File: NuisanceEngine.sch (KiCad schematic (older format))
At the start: 60 parts, among them J1 1/8\" Stereo, J2 CV_IN, J3 PWR_IN, J4 GND, J5 PWR_NORM, Q1 2N3904, Q2 2N3904, Q3 TIP31A, Q4 TIP32A, SW1 SW_SPDT, SW2 SW_SPDT, U1 LM324

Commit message: Made footprint for second model of battery holder
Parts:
- BT1: footprint (none) -> HammerheadAudio:9V_Clip
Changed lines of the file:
@@
 F 0 "BT1" H 10750 2200 50  0000 L CNN
 F 1 "9V_Battery" H 10750 2100 50  0000 L CNN
-F 2 "" V 10650 2160 50  0001 C CNN
+F 2 "HammerheadAudio:9V_Clip" V 10650 2160 50  0001 C CNN
 F 3 "" V 10650 2160 50  0001 C CNN
 	1    10650 2100

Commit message: Updated to Kicad 5... Very annoying >:/
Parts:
- removed J1: 1/8\" Stereo, HammerheadAudio:EuroJack_StereoTHT, symbol Audio-Jack-3
- removed J2: CV_IN, HammerheadAudio:EuroJack_MonoSW_THT, symbol Audio-Jack-2_Switch
- added J1, J8: GND, Connector_PinHeader_2.54mm:PinHeader_1x01_P2.54mm_Vertical, symbol Connector:Conn_01x01_Female
- added J2: CV, Connector_PinHeader_2.54mm:PinHeader_1x01_P2.54mm_Vertical, symbol Connector:Conn_01x01_Female
- added J6: L, Connector_PinHeader_2.54mm:PinHeader_1x01_P2.54mm_Vertical, symbol Connector:Conn_01x01_Female
- added J7: R, Connector_PinHeader_2.54mm:PinHeader_1x01_P2.54mm_Vertical, symbol Connector:Conn_01x01_Female
- added unit 5 of U1
- BT1: symbol Battery_Cell -> Device:Battery_Cell
- C1, C2, C3, C4, C5, C6, C7: symbol C -> Device:C
- C10, C11, C8, C9: symbol CP -> Device:CP
- D1: symbol D -> Device:D
- D2: symbol LED -> Device:LED
- J3: value PWR_IN -> 9V; footprint Pin_Headers:Pin_Header_Straight_1x01_Pitch2.54mm -> Connector_PinHeader_2.54mm:PinHeader_1x01_P2.54mm_Vertical; symbol Conn_01x01 -> Connector:Conn_01x01_Female
- J4: footprint Pin_Headers:Pin_Header_Straight_1x01_Pitch2.54mm -> Connector_PinHeader_2.54mm:PinHeader_1x01_P2.54mm_Vertical; symbol Conn_01x01 -> Connector:Conn_01x01_Female
- J5: value PWR_NORM -> BAT; footprint Pin_Headers:Pin_Header_Straight_1x01_Pitch2.54mm -> Connector_PinHeader_2.54mm:PinHeader_1x01_P2.54mm_Vertical; symbol Conn_01x01 -> Connector:Conn_01x01_Female
- LS1: symbol Speaker -> Device:Speaker
- Q1: symbol Q_NPN_EBC -> Device:Q_NPN_EBC
- Q2: symbol Q_NPN_EBC -> Transistor_BJT:2N3904
- Q3: symbol TIP41 -> Device:Q_NPN_BCE
- Q4: symbol Q_PNP_BCE -> Device:Q_PNP_BCE
- R1, R10, R11, R12, R13, R14, R15, R16, R17, R18, R19, R2, R20, R21, R22, R23, R24, R25, R26, R27, R29, R3, R4, R5, R6, R7, R8, R9: symbol R -> Device:R
- RV1, RV2, RV4, RV5: symbol POT -> Device:R_POT
- RV3: symbol POT_TRIM -> Device:R_POT_TRIM
- SW1, SW2: symbol SW_SPDT -> Switch:SW_SPDT
- U1: symbol LM324 -> Amplifier_Operational:LM324
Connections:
- wire segments 136 -> 165
- no-connect marks 1 -> 0

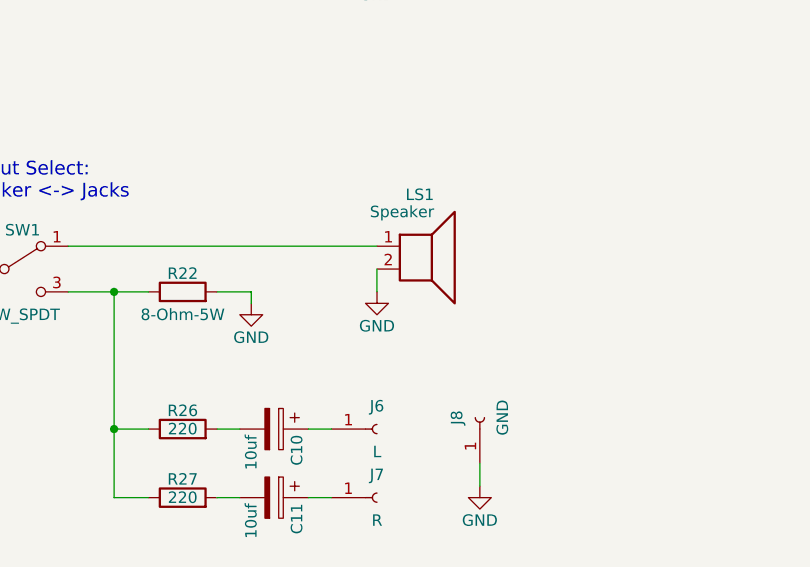
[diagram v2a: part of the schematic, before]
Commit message: Changed speaker connection
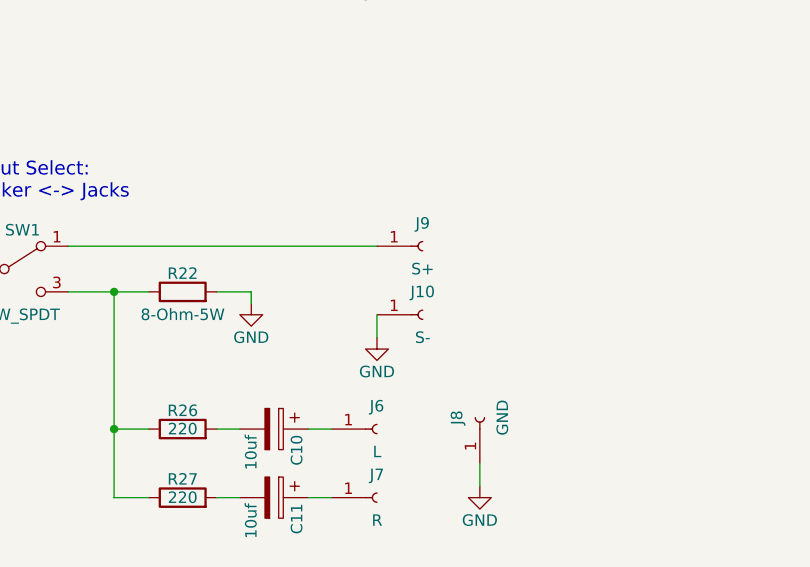
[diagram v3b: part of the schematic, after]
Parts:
- removed LS1: Speaker, Connectors_Molex:Molex_NanoFit_1x02x2.50mm_Straight, symbol Device:Speaker
- added J10: S-, Connector_PinHeader_2.54mm:PinHeader_1x01_P2.54mm_Vertical, symbol Connector:Conn_01x01_Female
- added J9: S+, Connector_PinHeader_2.54mm:PinHeader_1x01_P2.54mm_Vertical, symbol Connector:Conn_01x01_Female
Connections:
- net GND: now also J10.1 (Pin_1)
- net at SW1.1 (A): now also J9.1 (Pin_1)
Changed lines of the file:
@@
-$EndComp
-$Comp
-L Device:Speaker LS1
-U 1 1 5BD80D04
-P 8700 4250
-F 0 "LS1" H 8750 4475 50  0000 R CNN
-F 1 "Speaker" H 8750 4400 50  0000 R CNN
-F 2 "Connectors_Molex:Molex_NanoFit_1x02x2.50mm_Straight" H 8700 4050 50  0001 C CNN
-F 3 "" H 8690 4200 50  0001 C CNN
-	1    8700 4250
-	1    0    0    -1
 $EndComp
 $Comp
@@
 L power:GND #PWR027
 U 1 1 5BD80D37
-P 8500 4450
-F 0 "#PWR027" H 8500 4200 50  0001 C CNN
-F 1 "GND" H 8500 4300 50  0000 C CNN
-F 2 "" H 8500 4450 50  0001 C CNN
-F 3 "" H 8500 4450 50  0001 C CNN
-	1    8500 4450
+P 8500 4650
+F 0 "#PWR027" H 8500 4400 50  0001 C CNN
+F 1 "GND" H 8500 4500 50  0000 C CNN
+F 2 "" H 8500 4650 50  0001 C CNN
+F 3 "" H 8500 4650 50  0001 C CNN
+	1    8500 4650
 	-1   0    0    -1
 $EndComp
@@
 	7150 4250 8500 4250
 Wire Wire Line
-	8500 4450 8500 4350
+	8500 4650 8500 4550
 Wire Wire Line
 	7600 2200 7600 2100
@@
 Wire Wire Line
 	8500 3000 8500 2950
+$Comp
+L Connector:Conn_01x01_Female J9
+U 1 1 5C07A97F
+P 8700 4250
+F 0 "J9" H 8700 4350 50  0000 C CNN
+F 1 "S+" H 8700 4150 50  0000 C CNN
+F 2 "Connector_PinHeader_2.54mm:PinHeader_1x01_P2.54mm_Vertical" H 8700 4250 50  0001 C CNN
+F 3 "" H 8700 4250 50  0001 C CNN
+	1    8700 4250
+	1    0    0    -1
+$EndComp
+$Comp
+L Connector:Conn_01x01_Female J10
+U 1 1 5C07AB37
+P 8700 4550
+F 0 "J10" H 8700 4650 50  0000 C CNN
+F 1 "S-" H 8700 4450 50  0000 C CNN
+F 2 "Connector_PinHeader_2.54mm:PinHeader_1x01_P2.54mm_Vertical" H 8700 4550 50  0001 C CNN
+F 3 "" H 8700 4550 50  0001 C CNN
+	1    8700 4550
+	1    0    0    -1
+$EndComp
 $EndSCHEMATC

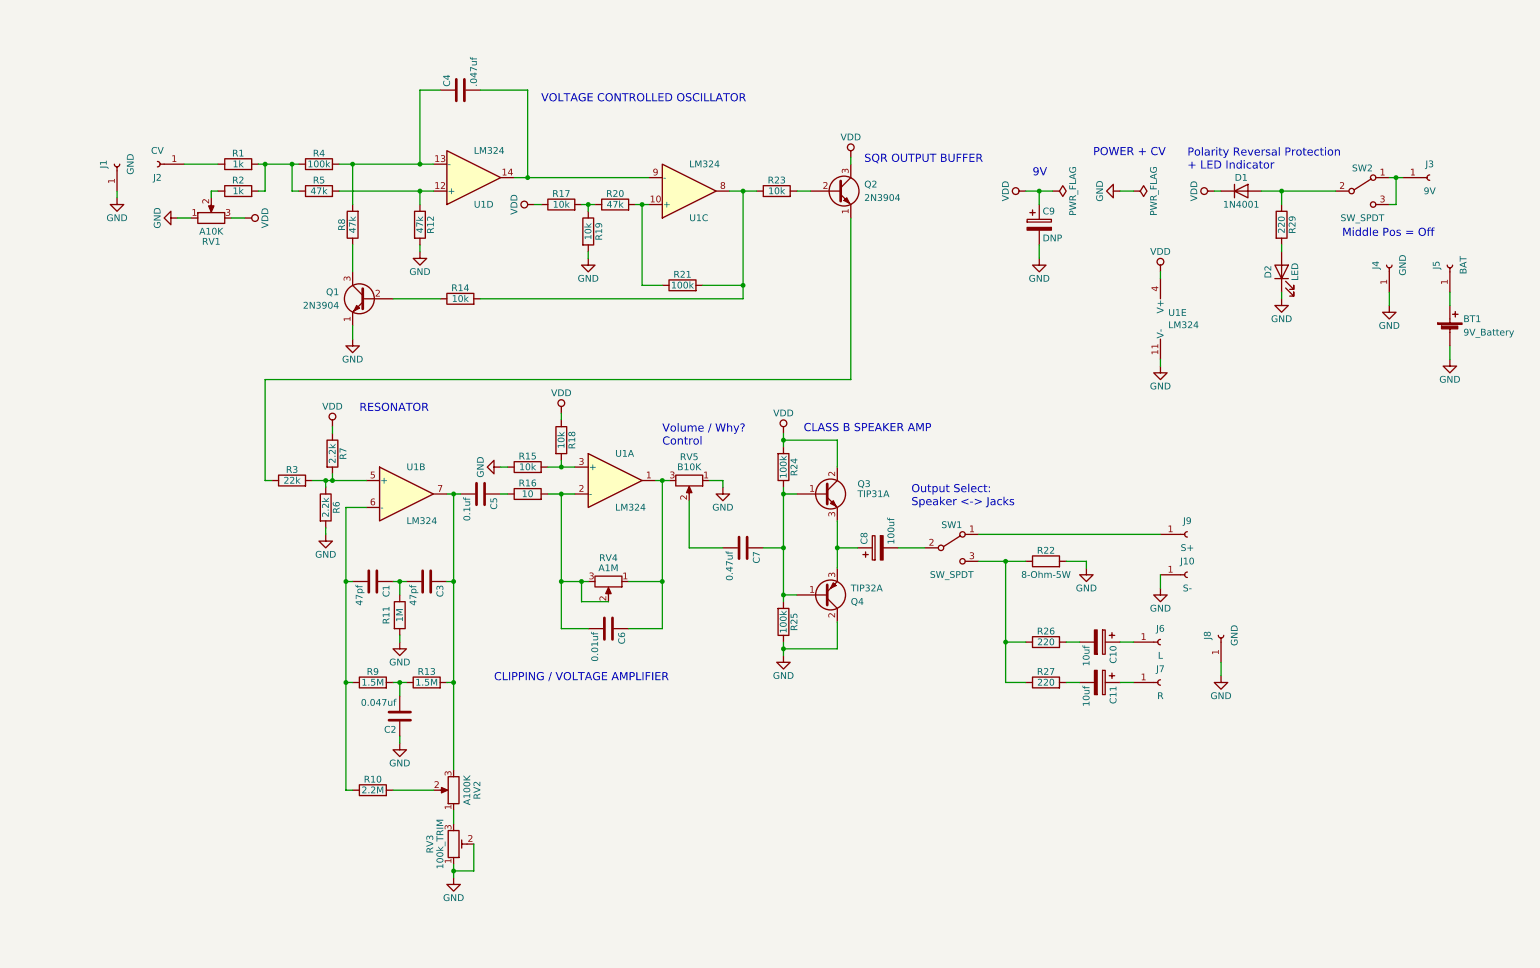
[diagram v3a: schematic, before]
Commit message: Updated pin headers
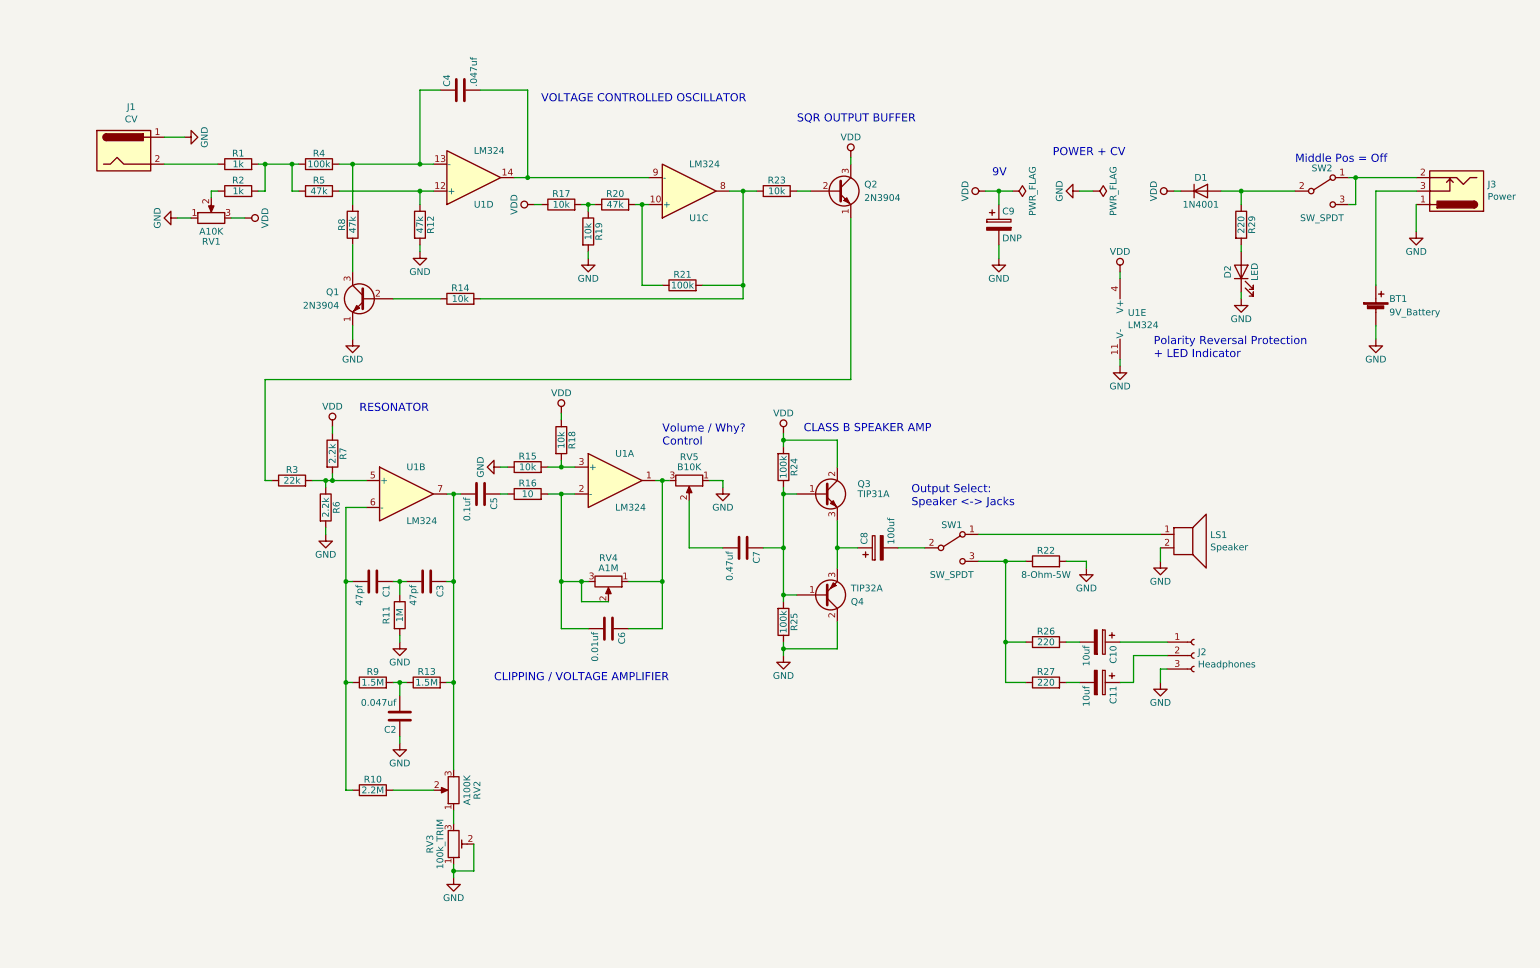
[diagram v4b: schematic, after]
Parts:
- removed J1, J4, J8: GND, Connector_PinHeader_2.54mm:PinHeader_1x01_P2.54mm_Vertical, symbol Connector:Conn_01x01_Female
- removed J10: S-, Connector_PinHeader_2.54mm:PinHeader_1x01_P2.54mm_Vertical, symbol Connector:Conn_01x01_Female
- removed J2: CV, Connector_PinHeader_2.54mm:PinHeader_1x01_P2.54mm_Vertical, symbol Connector:Conn_01x01_Female
- removed J3: 9V, Connector_PinHeader_2.54mm:PinHeader_1x01_P2.54mm_Vertical, symbol Connector:Conn_01x01_Female
- removed J5: BAT, Connector_PinHeader_2.54mm:PinHeader_1x01_P2.54mm_Vertical, symbol Connector:Conn_01x01_Female
- removed J6: L, Connector_PinHeader_2.54mm:PinHeader_1x01_P2.54mm_Vertical, symbol Connector:Conn_01x01_Female
- removed J7: R, Connector_PinHeader_2.54mm:PinHeader_1x01_P2.54mm_Vertical, symbol Connector:Conn_01x01_Female
- removed J9: S+, Connector_PinHeader_2.54mm:PinHeader_1x01_P2.54mm_Vertical, symbol Connector:Conn_01x01_Female
- added J1: CV, Connector_PinHeader_2.54mm:PinHeader_1x02_P2.54mm_Vertical, symbol Connector:Barrel_Jack
- added J2: Headphones, Connector_PinHeader_2.54mm:PinHeader_1x03_P2.54mm_Vertical, symbol Connector:Conn_01x03_Female
- added J3: Power, Connector_PinHeader_2.54mm:PinHeader_1x03_P2.54mm_Vertical, symbol Connector:Barrel_Jack_Switch
- added LS1: Speaker, Connector_PinHeader_2.54mm:PinHeader_1x02_P2.54mm_Vertical, symbol Device:Speaker
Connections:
- net GND: now also J1.1, J2.3 (Pin_3), J3.1, LS1.2
- net at R1.1: now also J1.2
- net at SW2.1 (A), SW2.3 (C): now also J3.2
- net at C10.1: now also J2.1 (Pin_1)
- net at C11.1: now also J2.2 (Pin_2)
- net at BT1.1 (+): now also J3.3
- net at SW1.1 (A): now also LS1.1
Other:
- moved on the sheet: BT1, C9, D1, D2, R29, SW2, U1E

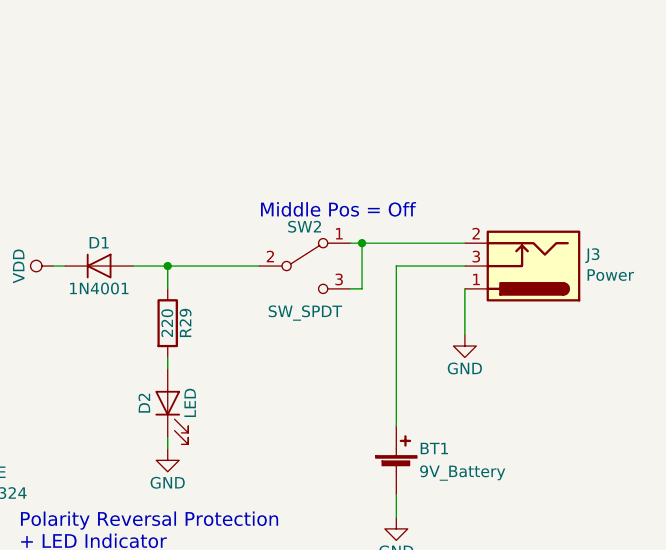
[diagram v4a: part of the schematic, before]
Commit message: Started basic layout
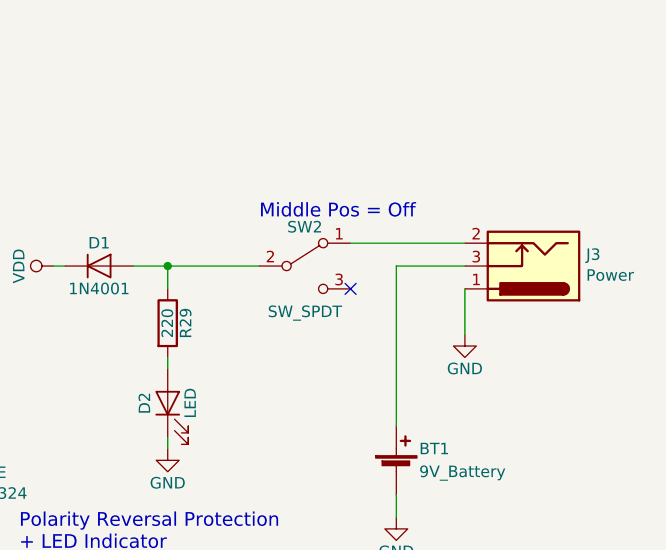
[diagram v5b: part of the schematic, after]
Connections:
- net at J3.2, SW2.1 (A): no longer SW2.3 (C)
- no-connect marks 0 -> 1
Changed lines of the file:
@@
 	7950 4450 7950 4500
-Wire Wire Line
-	9900 1600 9950 1600
-Wire Wire Line
-	9900 1800 9950 1800
-Wire Wire Line
-	9950 1800 9950 1600
-Connection ~ 9950 1600
 Wire Wire Line
 	8950 1700 9100 1700
@@
 	8500 5250 8550 5250
 Wire Wire Line
-	9950 1600 10400 1600
-Wire Wire Line
 	10400 1800 10400 2000
 Wire Wire Line
@@
 	-1   0    0    1
 $EndComp
+Wire Wire Line
+	9900 1600 10400 1600
+NoConn ~ 9900 1800
 $EndSCHEMATC

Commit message: More mushing
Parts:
- C10, C11: footprint Capacitors_THT:CP_Radial_D6.3mm_P2.50mm -> Capacitor_THT:CP_Radial_D5.0mm_P2.00mm
- C8: footprint Capacitors_THT:CP_Radial_D6.3mm_P2.50mm -> Capacitor_THT:CP_Radial_D6.3mm_P2.50mm
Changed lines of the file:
@@
 F 0 "C8" H 6425 4450 50  0000 L CNN
 F 1 "100uf" H 6425 4250 50  0000 L CNN
-F 2 "Capacitors_THT:CP_Radial_D6.3mm_P2.50mm" H 6438 4200 50  0001 C CNN
+F 2 "Capacitor_THT:CP_Radial_D6.3mm_P2.50mm" H 6438 4200 50  0001 C CNN
 F 3 "" H 6400 4350 50  0001 C CNN
 	1    6400 4350
@@
 F 0 "C10" H 8075 5150 50  0000 L CNN
 F 1 "10uf" H 8075 4950 50  0000 L CNN
-F 2 "Capacitors_THT:CP_Radial_D6.3mm_P2.50mm" H 8088 4900 50  0001 C CNN
+F 2 "Capacitor_THT:CP_Radial_D5.0mm_P2.00mm" H 8088 4900 50  0001 C CNN
 F 3 "" H 8050 5050 50  0001 C CNN
 	1    8050 5050
@@
 F 0 "C11" H 8075 5450 50  0000 L CNN
 F 1 "10uf" H 8075 5250 50  0000 L CNN
-F 2 "Capacitors_THT:CP_Radial_D6.3mm_P2.50mm" H 8088 5200 50  0001 C CNN
+F 2 "Capacitor_THT:CP_Radial_D5.0mm_P2.00mm" H 8088 5200 50  0001 C CNN
 F 3 "" H 8050 5350 50  0001 C CNN
 	1    8050 5350

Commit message: Switched to SMT footprints
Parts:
- C1, C2, C3, C4, C5, C6: footprint Capacitors_THT:C_Disc_D5.0mm_W2.5mm_P2.50mm -> Capacitor_SMD:C_0603_1608Metric_Pad1.05x0.95mm_HandSolder
- C10, C11: footprint Capacitor_THT:CP_Radial_D5.0mm_P2.00mm -> Resistor_SMD:R_0805_2012Metric_Pad1.15x1.40mm_HandSolder
- C7: footprint Capacitors_THT:C_Disc_D5.0mm_W2.5mm_P5.00mm -> Capacitor_SMD:C_0805_2012Metric_Pad1.15x1.40mm_HandSolder
- C9: footprint Capacitors_THT:CP_Radial_D5.0mm_P2.00mm -> Resistor_SMD:R_0805_2012Metric_Pad1.15x1.40mm_HandSolder
- D1: footprint Diodes_THT:D_DO-41_SOD81_P7.62mm_Horizontal -> Diode_SMD:D_SMA_Handsoldering
- Q1, Q2: footprint TO_SOT_Packages_THT:TO-92_Inline_Wide -> Package_TO_SOT_SMD:SOT-23_Handsoldering
- Q3, Q4: footprint TO_SOT_Packages_THT:TO-220_Vertical -> Package_TO_SOT_THT:TO-220-3_Horizontal_TabDown
- R1, R10, R11, R12, R13, R14, R15, R16, R17, R18, R19, R2, R20, R21, R23, R24, R25, R26, R27, R29, R3, R4, R5, R6, R7, R8, R9: footprint Resistors_THT:Resistor_Horizontal_RM7mm -> Resistor_SMD:R_0603_1608Metric_Pad1.05x0.95mm_HandSolder

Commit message: Commit before changing pot footprint
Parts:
- C4: value .047uf -> 0.047uf
- Q1: symbol Device:Q_NPN_EBC -> Device:Q_NPN_BEC
- Q2: symbol Transistor_BJT:2N3904 -> Device:Q_NPN_BEC
- R22: value 8-Ohm-5W -> 4-Ohm-5W
- RV5: value B10K -> C10K
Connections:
- net GND: now also Q1.2 (E); no longer Q1.1 (E)
- net at R14.1: now also Q1.1 (B); no longer Q1.2 (B)
- net at R23.2: now also Q2.1 (B); no longer Q2.2 (B)
- net at R3.1: now also Q2.2 (E); no longer Q2.1 (E)
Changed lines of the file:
@@
 EESchema Schematic File Version 4
 LIBS:NuisanceEngine-cache
-EELAYER 26 0
+EELAYER 29 0
 EELAYER END
 $Descr A4 11693 8268
@@
 P 3300 950
 F 0 "C4" H 3325 1050 50  0000 L CNN
-F 1 ".047uf" H 3325 850 50  0000 L CNN
+F 1 "0.047uf" H 3325 850 50  0000 L CNN
 F 2 "Capacitor_SMD:C_0603_1608Metric_Pad1.05x0.95mm_HandSolder" H 3338 800 50  0001 C CNN
 F 3 "" H 3300 950 50  0001 C CNN
@@
 $EndComp
 $Comp
-L Device:Q_NPN_EBC Q1
+L Device:Q_NPN_BEC Q1
 U 1 1 5BD80CF7
 P 2600 2500
@@
 9V
 $Comp
-L Transistor_BJT:2N3904 Q2
+L Device:Q_NPN_BEC Q2
 U 1 1 5BD80D0B
 P 6100 1700
@@
 P 7650 4450
 F 0 "R22" V 7730 4450 50  0000 C CNN
-F 1 "8-Ohm-5W" V 7550 4450 50  0000 C CNN
+F 1 "4-Ohm-5W" V 7550 4450 50  0000 C CNN
 F 2 "HammerheadAudio:Resistor_Vishay5W" V 7580 4450 50  0001 C CNN
 F 3 "" H 7650 4450 50  0001 C CNN
@@
 Wire Wire Line
 	7950 4450 7950 4500
-Wire Wire Line
-	8950 1700 9100 1700
 $Comp
 L Device:CP C10
@@
 P 5000 3850
 F 0 "RV5" V 4825 3850 50  0000 C CNN
-F 1 "B10K" V 4900 3850 50  0000 C CNN
+F 1 "C10K" V 4900 3850 50  0000 C CNN
 F 2 "HammerheadAudio:Alpha_Pot_16MM" H 5000 3850 50  0001 C CNN
 F 3 "" H 5000 3850 50  0001 C CNN
@@
 $EndComp
 Wire Wire Line
-	9100 1800 9100 1700
-Connection ~ 9100 1700
-Wire Wire Line
 	8600 1700 8650 1700
 Text Notes 8450 2950 0    60   ~ 0
@@
 Wire Wire Line
 	7300 1700 7400 1700
-Wire Wire Line
-	9100 1700 9500 1700
 Wire Wire Line
 	7350 4450 7500 4450
@@
 	9900 1600 10400 1600
 NoConn ~ 9900 1800
+$Comp
+L Graphic:SYM_Hot_Small #SYM1
+U 1 1 5CB9FDAB
+P 9600 6350
+F 0 "#SYM1" H 9600 6490 50  0001 C CNN
+F 1 "SYM_Hot_Small" H 9600 6225 50  0001 C CNN
+F 2 "" H 9600 6175 50  0001 C CNN
+F 3 "~" H 9630 6150 50  0001 C CNN
+	1    9600 6350
+	1    0    0    -1
+$EndComp
+Wire Wire Line
+	9100 1800 9100 1700
+Wire Wire Line
+	8950 1700 9100 1700
+Connection ~ 9100 1700
+Wire Wire Line
+	9100 1700 9500 1700
 $EndSCHEMATC
